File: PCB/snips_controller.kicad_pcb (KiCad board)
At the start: 4 copper layers, 35 x 99.9 mm, 84 parts

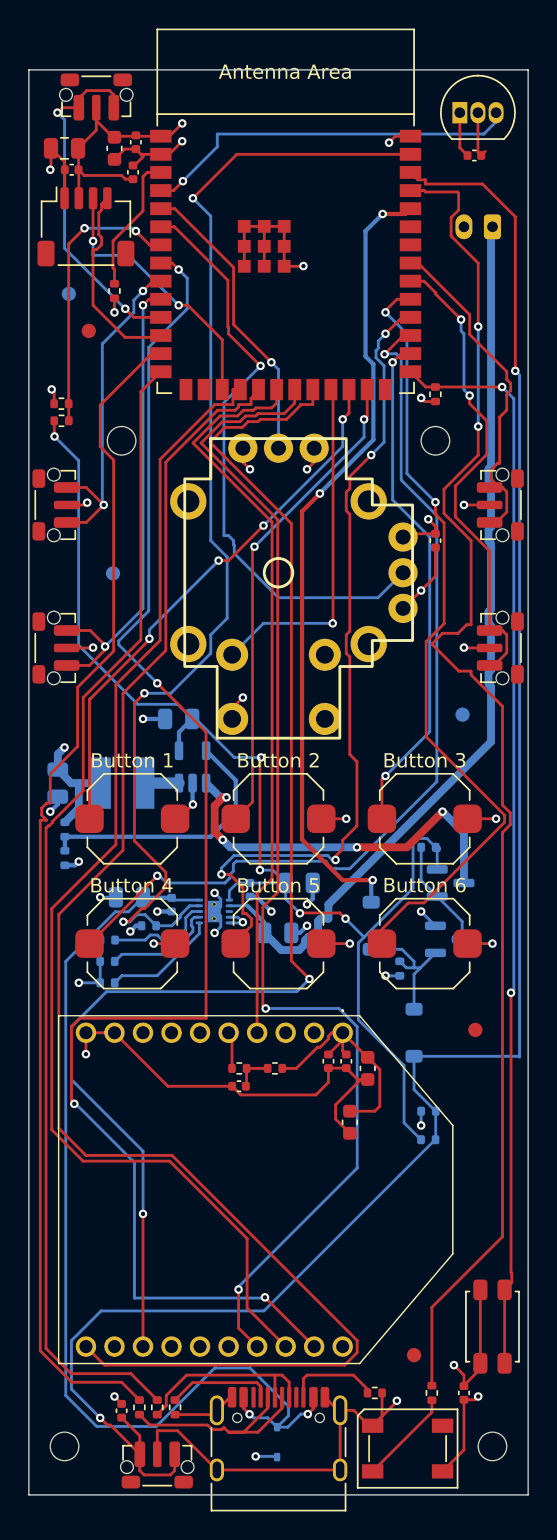
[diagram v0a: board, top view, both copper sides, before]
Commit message: refactor: added STAT2
It was worth adding and will give us more info during battery charging.
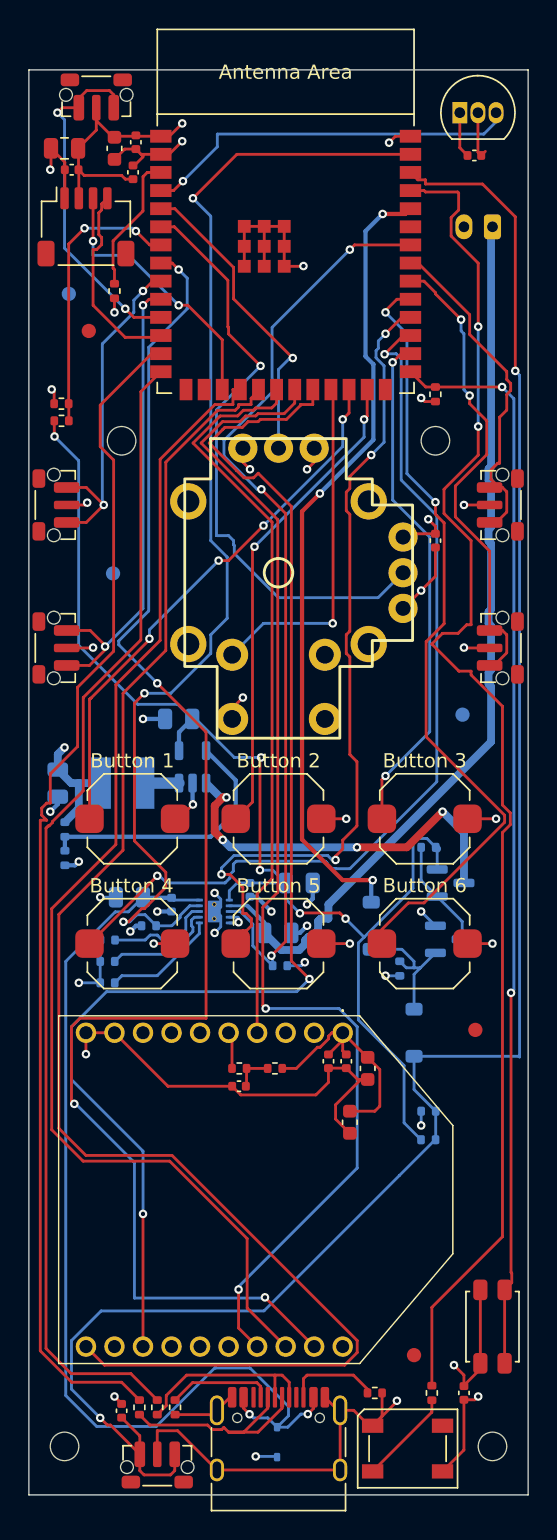
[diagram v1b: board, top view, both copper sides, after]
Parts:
- added R_STAT2: 10kΩ, Resistor_SMD:R_0402_1005Metric, B.Cu at (137.6, 122.8)
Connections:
- U_CHG1 pad 3: unconnected-(U_CHG1-STAT2-Pad3) -> /MCU_Core/STAT2
- U_MCU1 pad 34: unconnected-(U_MCU1-MTDI/GPIO41/CLK_OUT1-Pad34) -> /MCU_Core/STAT2
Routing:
- net /MCU_Core/STAT2: track 0.00 -> 66.2 mm, vias 0 -> 3
- net 3V3: track 56.0 -> 57.4 mm, vias 9 -> 10
- net /MCU_Core/XBEE_ON_SLEEP: track 92.5 -> 93.6 mm
- net /MCU_Core/STICK_X: track 20.8 -> 21.7 mm
- net /MCU_Core/STICK_Y: track 41.7 -> 42.5 mm

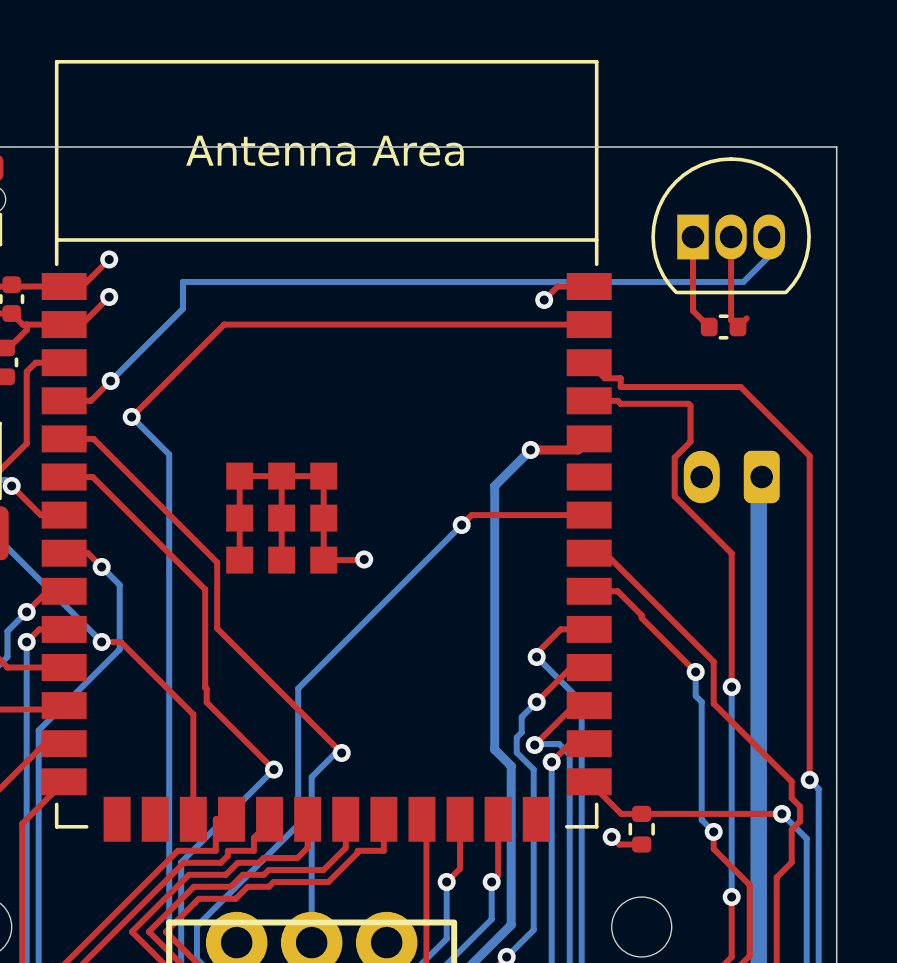
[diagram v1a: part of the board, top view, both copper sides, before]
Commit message: refactor: flipped hall sensor to back side
This is a better position for the hall trigger anyway.
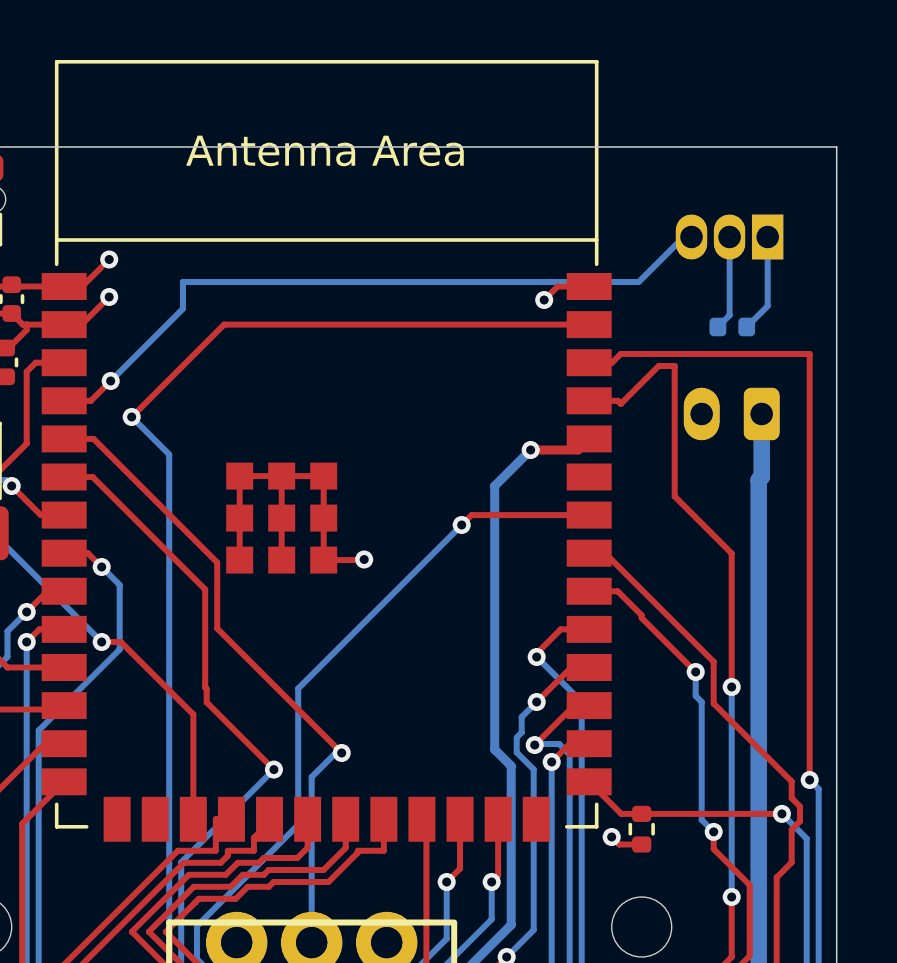
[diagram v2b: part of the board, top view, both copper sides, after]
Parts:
- C_HALL1, U_HALL1: moved to B.Cu
- moved U_HALL1 2.49 mm to (152.7, 63.0), turned to 180 degrees
- moved BT1 2.10 mm to (152.5, 68.9)
- moved C_HALL1 0.29 mm to (151.5, 66.0), turned to 180 degrees
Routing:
- net /Hall_Trigger/TRIG_ANALOG: track 26.7 -> 23.7 mm
- net VBAT: track 63.9 -> 66.0 mm
- net /MCU_Core/PWR_BTN_SENSE: track 130.8 -> 132.8 mm
- net /MCU_Core/RGB_DIN: track 96.9 -> 97.9 mm
- net 3V3: track 57.4 -> 58.1 mm
